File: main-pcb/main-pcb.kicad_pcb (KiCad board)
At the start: 10 copper layers, 130 x 90 mm, 444 parts, among them J1 CONN_01X03, J10 CONN_DUMPTRUCK_HOST, J11 CONN_01X03, J12 PMOD_HOST, J13 PMOD_HOST, J14 USB_C_Receptacle_USB2.0, J2 CORTEX_DEBUG_ETM, J3 XILINX_JTAG, J4 CORTEX_DEBUG_ETM, J5 CONN_01X03, J6 0826-1G1T-23-F, J7 CONN_DUMPTRUCK_HOST, J8 CONN_DUMPTRUCK_HOST, J9 CONN_DUMPTRUCK_HOST, M1 MECHANICAL, M2 SCREWHOLE, M3 SCREWHOLE, M4 SCREWHOLE, M5 SCREWHOLE, M6 MECHANICAL, M7 MECHANICAL, M8 MECHANICAL, M9 MECHANICAL, Q1 SSM6N58NU, SW1 SWITCH, SW2 SWITCH, U1 XC7S100-1FGGA484C, U10 NCP45525IMNTWG-H, U11 LTC3374-QFN, U12 AT24MAC402, U13 ECS-1612MV-250-CN, U14 STM32H735-UFBGA176-25, U15 S27KL0642GABHB020, U16 ECS-1612MV-250-CN, U17 S27KS0642GABHI030, U18 ECS-1612MV-250-CN, U19 INA230, U2 STM32L431-QFN48, U20 KSZ9031RN, U21 RCLAMP0514M, U22 RCLAMP0514M, U23 NCP45525IMNTWG-H, U24 IS25WP256D-JLLE, U25 INA230, U26 74LVC1T45, U27 NCP45525IMNTWG-H, U28 INA230, U29 NCP45525IMNTWG-H, U3 INA230, U30 INA230, U31 NCP45525IMNTWG-H, U32 INA230, U33 19-C47/RSGHBHC-5V01/2T, U34 19-C47/RSGHBHC-5V01/2T, U35 19-C47/RSGHBHC-5V01/2T, U36 19-C47/RSGHBHC-5V01/2T, U37 19-C47/RSGHBHC-5V01/2T, U38 19-C47/RSGHBHC-5V01/2T, U39 NCP45525IMNTWG-H, U4 INA230, U5 INA230, U6 INA230, U7 INA230, U8 INA230, U9 INA230

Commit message: Continued layout, added first ground plane layer. 26 nets unrouted, still need to place last two INA230s
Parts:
- C10, C12: moved to B.Cu
- moved U6 39.5 mm to (148.4, 77.8), turned to 90 degrees
- moved C12 37.4 mm to (147.0, 77.2), turned to -90 degrees
- moved U4 31.3 mm to (153.2, 77.8), turned to 90 degrees
- moved C10 31.2 mm to (151.8, 76.2), turned to 90 degrees
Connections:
- U2 pad 26: /Power supply/SOFT_RST -> /Power supply/SOFT_PWR
- U2 pad 27: /Power supply/SOFT_PWR -> /Power supply/SOFT_RST
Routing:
- net /DUT_VCCIO_EN: track 153.1 -> 217.8 mm, vias 8 -> 9
- net /INA_ALERT: track 217.6 -> 262.1 mm, vias 10 -> 12
- net /SUPER_I2C_SCL: track 267.6 -> 309.3 mm, vias 12 -> 15
- net /SUPER_I2C_SDA: track 265.2 -> 306.3 mm, vias 13 -> 15
- net /Power supply/SOFT_PWR: track 65.5 -> 94.3 mm, vias 0 -> 2
- net /Power supply/SOFT_RST: track 58.3 -> 85.4 mm, vias 0 -> 2
- net /3V3_SB: track 464.9 -> 492.0 mm, vias 38 -> 43
- net /Power supply/2V5_SHIN: track 1.47 -> 15.5 mm, vias 3 -> 4
- net /2V5: track 226.3 -> 238.8 mm, vias 28 -> 29
- net /GND: track 2021.1 -> 2032.3 mm, vias 728 -> 741
- net /Power supply/3V3_SB_FB: track 1.30 -> 11.9 mm, vias 1 -> 2
- net /Power supply/3V3_SB_SHIN: track 1.46 -> 8.23 mm, vias 5 -> 6
- net /3V3: track 651.3 -> 647.9 mm
- net /VBUS_SHOUT: track 253.2 -> 252.4 mm
- net /1V0: track 108.9 -> 108.1 mm
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- added copper zone on In1.Cu, net /GND

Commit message: Updating file: main-pcb with current completely routed design
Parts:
- C13, C14: moved to B.Cu
- moved U7 34.5 mm to (148.5, 71.2)
- moved C13 31.9 mm to (150.0, 69.8)
- moved U8 26.4 mm to (153.5, 71.2)
- moved C14 23.4 mm to (154.8, 69.8)
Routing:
- net /1V2: track 246.7 -> 280.0 mm, vias 23 -> 24
- net /Power supply/1V2_SHIN: track 1.54 -> 32.2 mm, vias 3 -> 4
- net /1V8: track 315.6 -> 337.1 mm, vias 67 -> 69
- net /Power supply/1V8_SHIN: track 1.18 -> 21.4 mm, vias 3 -> 5
- net /3V3_SB: track 492.0 -> 509.6 mm, vias 43 -> 48
- net /INA_ALERT: track 262.1 -> 274.7 mm, vias 12 -> 13
- net /GND: track 2032.3 -> 2044.8 mm, vias 741 -> 754
- net /SUPER_I2C_SDA: track 306.3 -> 316.8 mm, vias 15 -> 17
- net /SUPER_I2C_SCL: track 309.3 -> 319.0 mm, vias 15 -> 17
- net /2V5: track 238.8 -> 239.8 mm, vias 29 -> 30

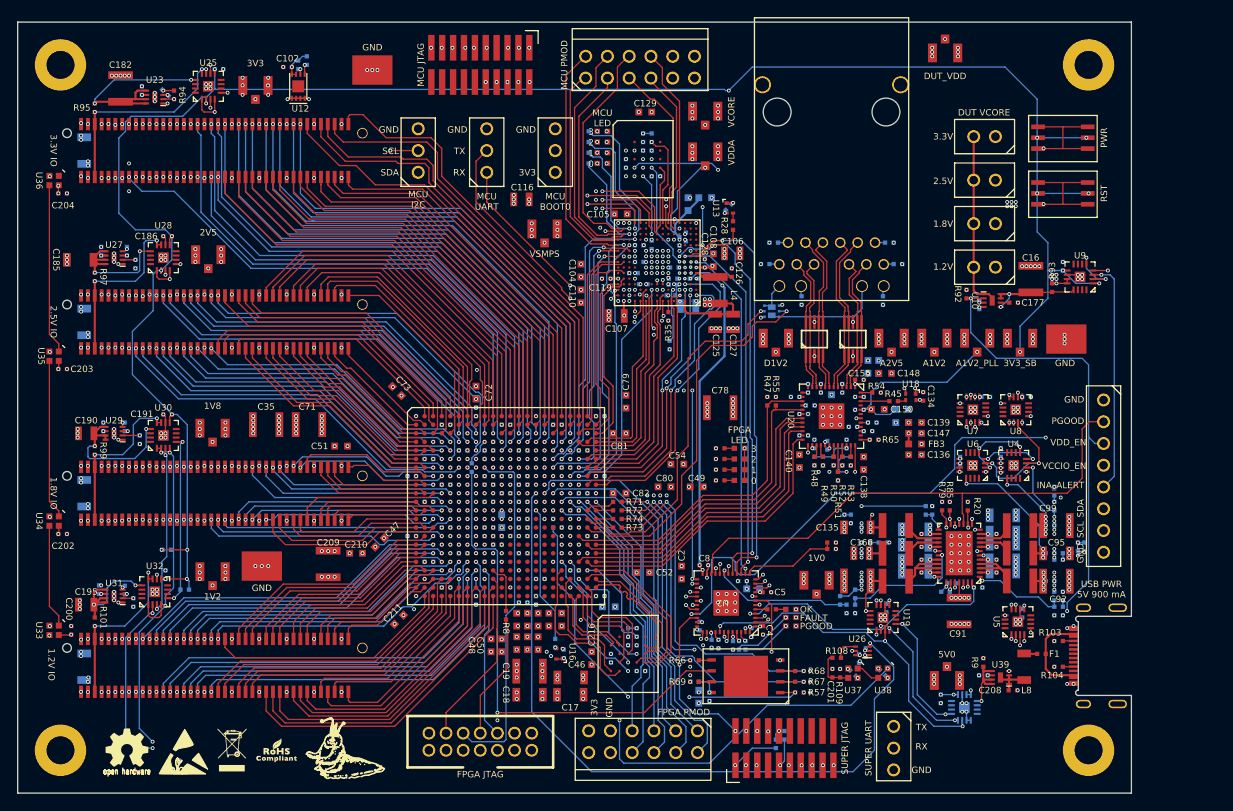
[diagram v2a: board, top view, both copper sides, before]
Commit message: Routing cleanup around MCU, fixed some DRC errors
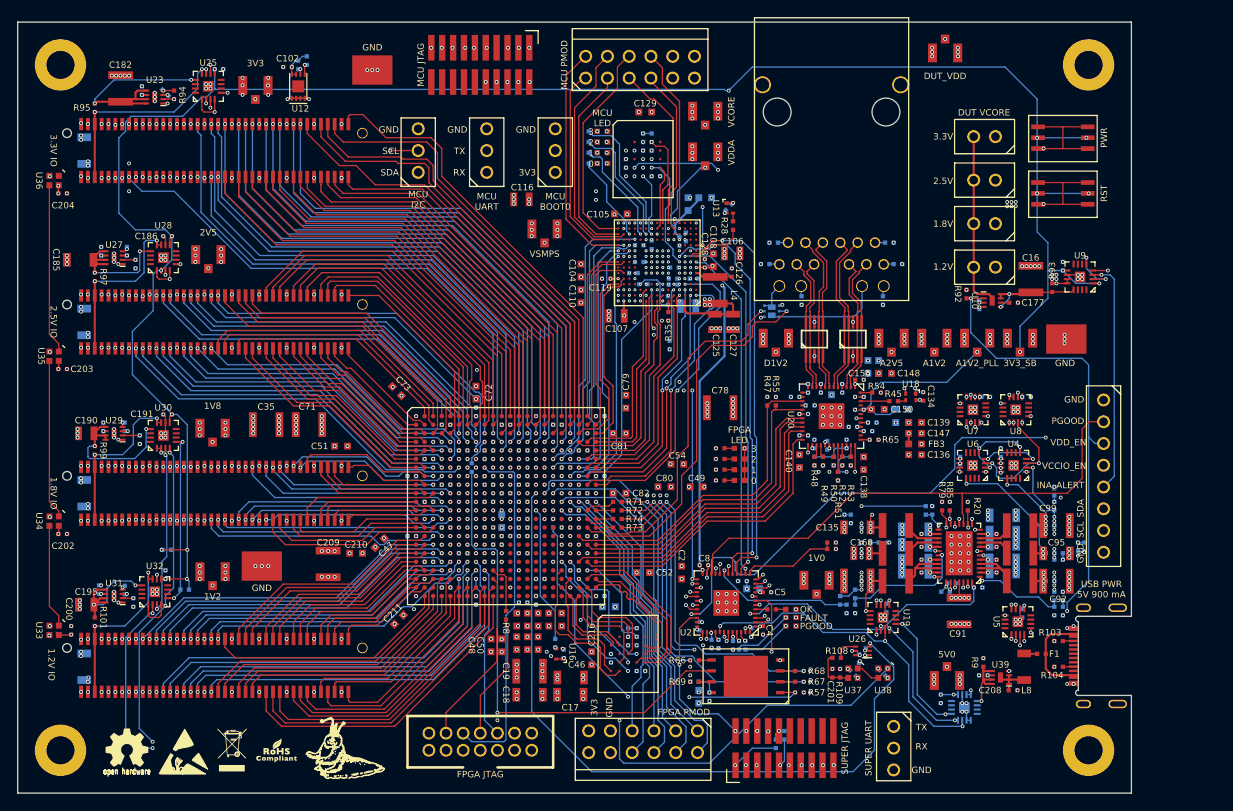
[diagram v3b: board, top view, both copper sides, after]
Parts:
- moved R32 0.69 mm to (112.9, 58.5), turned to 90 degrees
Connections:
- U1 pad F18: /MCU/FMC_AD14 -> /MCU/FMC_AD13
- U1 pad F20: /MCU/FMC_AD10 -> /MCU/FMC_AD15
- U1 pad G16: /MCU/FMC_AD6 -> /MCU/FMC_AD8
- U1 pad G17: /MCU/FMC_A17 -> /MCU/FMC_AD10
- U1 pad G20: /MCU/FMC_AD13 -> /MCU/FMC_AD14
- U1 pad H16: /MCU/FMC_AD5 -> /MCU/FMC_AD6
- U1 pad H17: /MCU/FMC_AD4 -> /MCU/FMC_AD12
- U1 pad H18: /MCU/FMC_AD9 -> /MCU/FMC_AD5
- U1 pad H19: /MCU/FMC_AD15 -> /MCU/FMC_A17
- U1 pad J16: /MCU/FMC_AD8 -> /MCU/FMC_AD4
- U1 pad J17: /MCU/FMC_AD12 -> /MCU/FMC_AD9
- U14 pad N10: unconnected-(U14F-PF15-PadN10) -> /MCU/MCU_LED_2
- U14 pad N11: unconnected-(U14F-PF13-PadN11) -> /MCU/MCU_LED_1
- U14 pad N12: /MCU/MCU_LED_3 -> unconnected-(U14B-PB10-PadN12)
- U14 pad P12: /MCU/MCU_LED_2 -> unconnected-(U14E-PE12-PadP12)
- U14 pad P13: /MCU/MCU_LED_1 -> unconnected-(U14E-PE13-PadP13)
- U14 pad R10: unconnected-(U14F-PF14-PadR10) -> /MCU/MCU_LED_3
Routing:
- net /MCU/FMC_AD5: track 47.2 -> 35.9 mm
- net /MCU/MCU_HYPERRAM_DQ7: track 24.5 -> 16.7 mm
- net /MCU/FMC_AD8: track 40.9 -> 34.4 mm
- net /MCU/FMC_AD7: track 46.8 -> 40.7 mm
- net /MCU/FMC_AD4: track 43.0 -> 37.8 mm
- net /MCU/MCU_HYPERRAM_DQ6: track 19.2 -> 14.3 mm
- net /3V3: track 647.9 -> 652.7 mm
- net /MCU/FMC_AD9: track 43.1 -> 39.6 mm
- net /MCU/FMC_AD6: track 40.8 -> 37.4 mm
- net /MCU/MCU_JTAG_TCK: track 38.7 -> 35.4 mm
- net /MCU/FMC_AD12: track 36.0 -> 33.1 mm
- net /MCU/FMC_AD10: track 28.8 -> 31.7 mm
- net /MCU/MCU_JTAG_TMS: track 36.5 -> 33.7 mm
- net /I2C_SCL: track 208.4 -> 206.1 mm
- net /I2C_SDA: track 209.2 -> 206.9 mm
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- added copper zone on In4.Cu, net /DUT_VDD
- added copper zone on In4.Cu, net /MCU/VCORE
- added copper zone on In4.Cu, net /MCU/VSMPS
